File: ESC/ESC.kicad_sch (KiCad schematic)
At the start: 28 parts, among them J1 Screw_Terminal_01x05, J2 Screw_Terminal_01x03, J3 Screw_Terminal_01x02, Q1 IPP060N06N, Q2 IPP060N06N, Q3 IPP060N06N, Q4 IPP060N06N, Q5 IPP060N06N, Q6 IPP060N06N, Q7 BS250, U6 LM7805_TO220

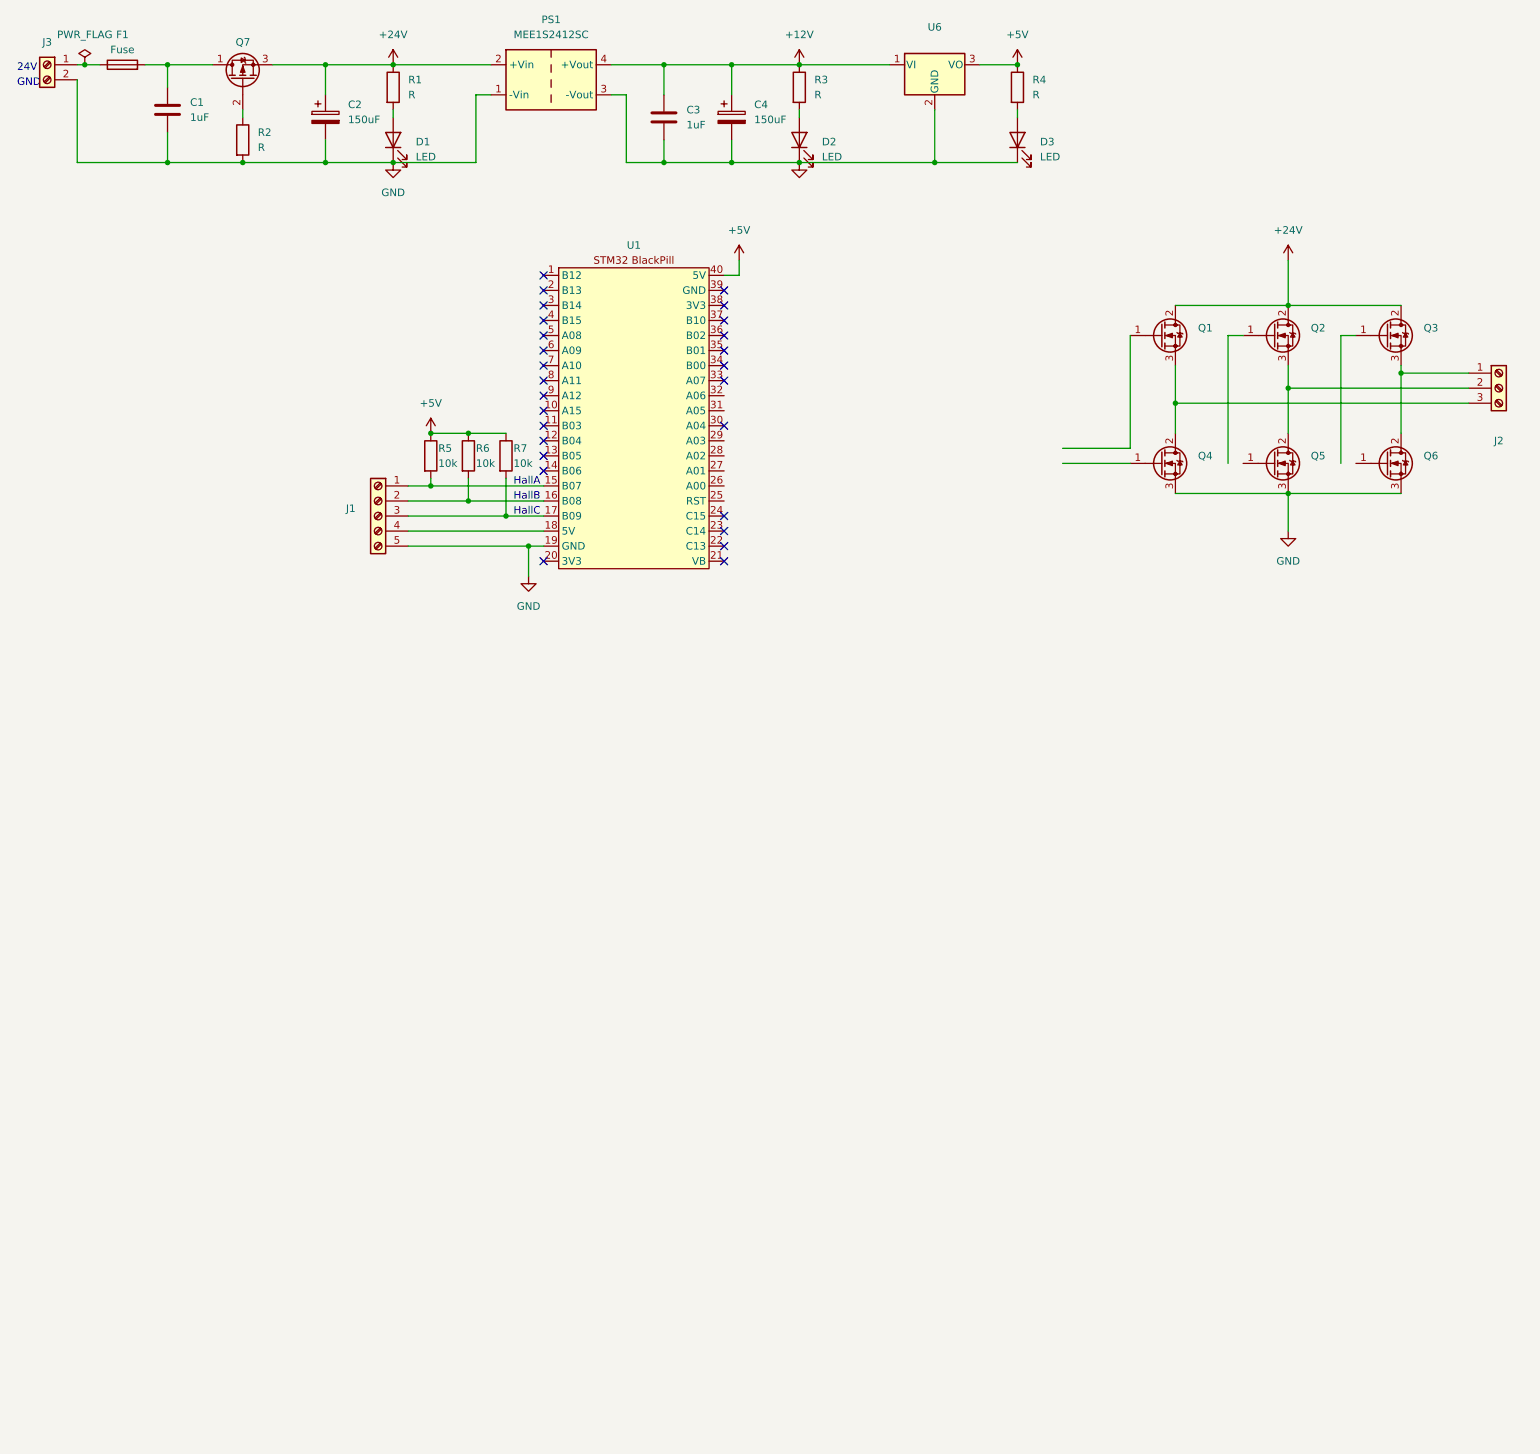
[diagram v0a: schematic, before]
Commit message: Added DRV8302
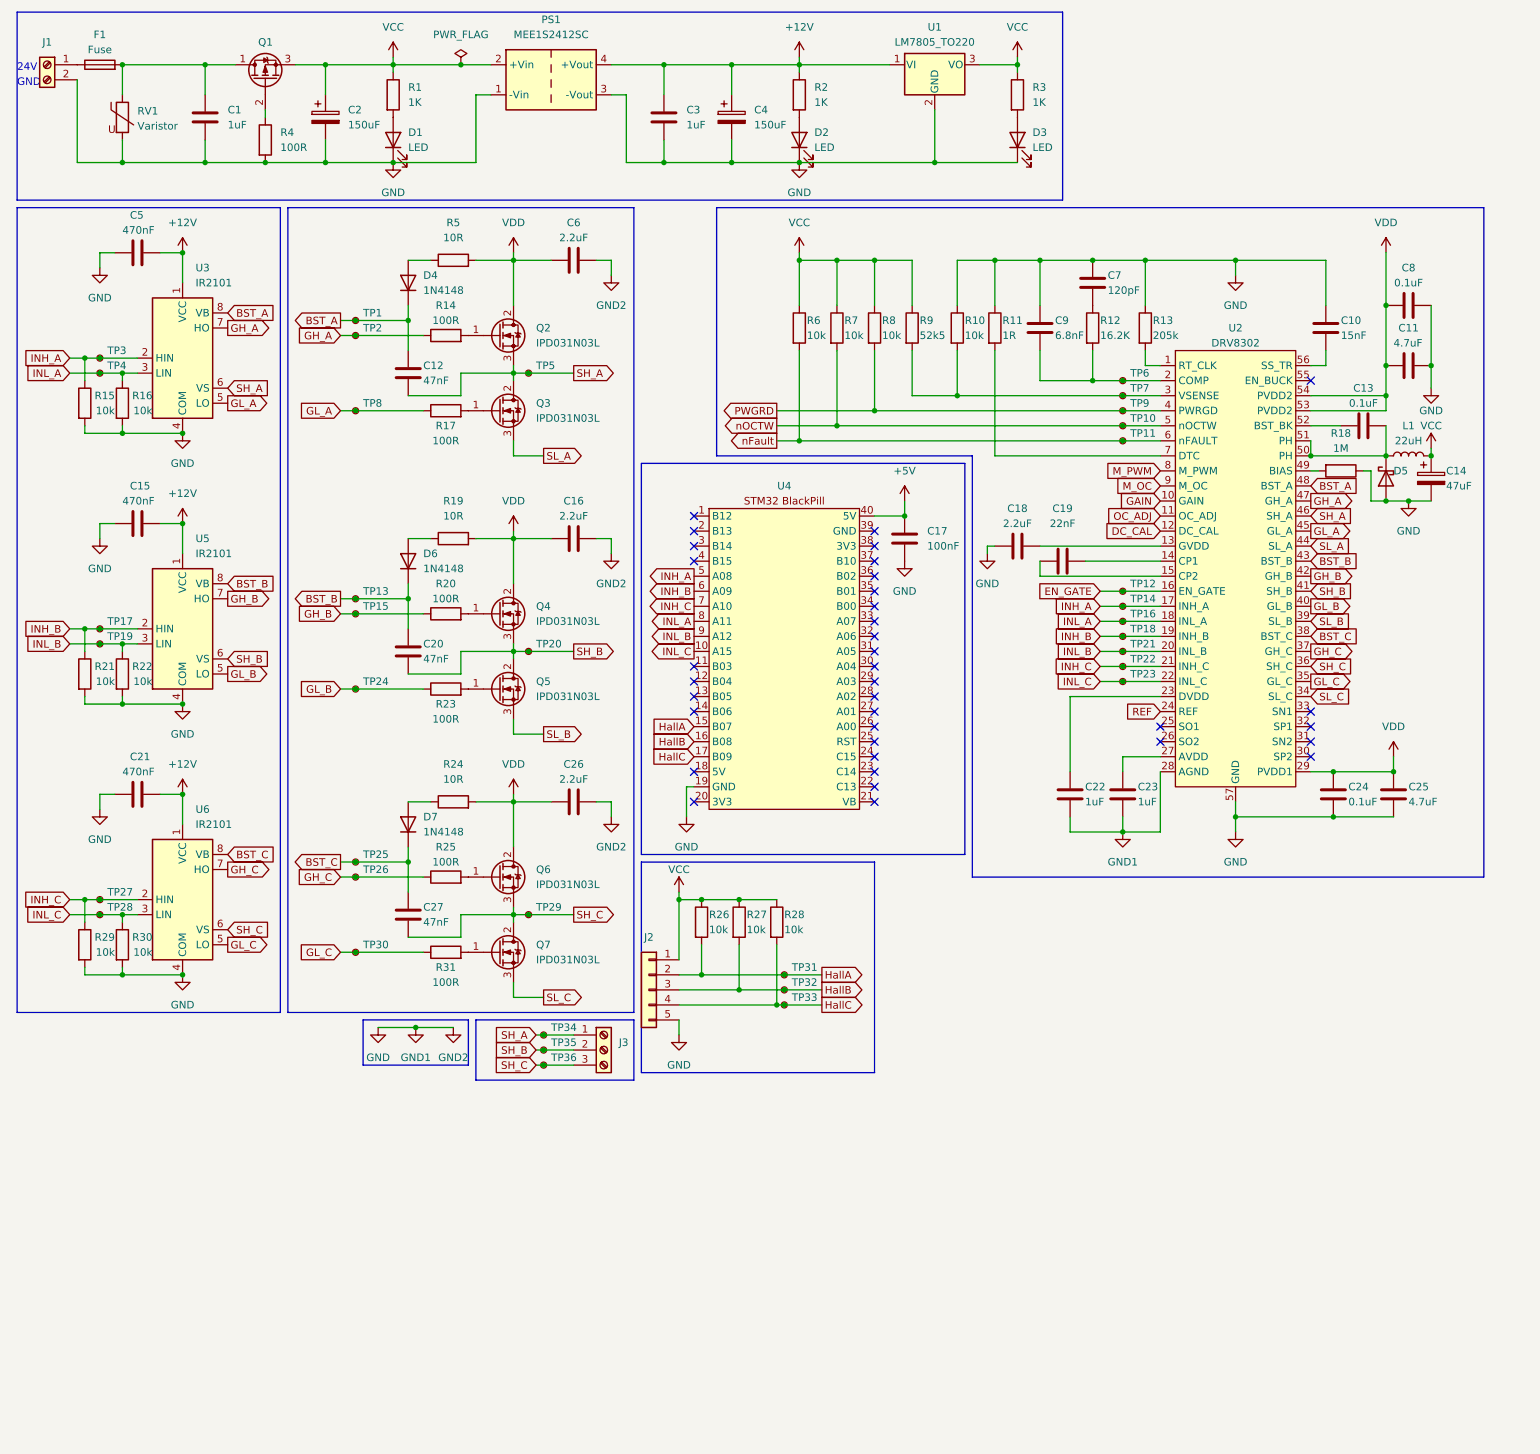
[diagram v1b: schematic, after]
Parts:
- removed J1: Screw_Terminal_01x05, symbol Connector:Screw_Terminal_01x05
- removed J2: Screw_Terminal_01x03, symbol Connector:Screw_Terminal_01x03
- removed Q1: IPP060N06N, Package_TO_SOT_THT:TO-220-3_Vertical, symbol Transistor_FET:IPP060N06N
- added C10: 15nF, symbol Device:C
- added C11, C25: 4.7uF, symbol Device:C
- added C12, C20, C27: 47nF, symbol Device:C
- added C13, C24, C8: 0.1uF, symbol Device:C
- added C14: 47uF, symbol Device:C_Polarized
- added C15, C21, C5: 470nF, symbol Device:C
- added C16, C18, C26, C6: 2.2uF, symbol Device:C
- added C17: 100nF, symbol Device:C
- added C19: 22nF, symbol Device:C
- added C22, C23: 1uF, symbol Device:C
- added C7: 120pF, symbol Device:C
- added C9: 6.8nF, symbol Device:C
- added D4, D6, D7: 1N4148, Diode_THT:D_DO-35_SOD27_P7.62mm_Horizontal, symbol Diode:1N4148
- added D5: D_Schottky, symbol Device:D_Schottky
- added J2: Conn_01x05, Connector_PinHeader_2.54mm:PinHeader_1x05_P2.54mm_Vertical, symbol Connector_Generic:Conn_01x05
- added J3: Screw_Terminal_01x03, symbol Connector:Screw_Terminal_01x03
- added L1: 22uH, symbol Device:L
- added Q7: IPD031N03L, Package_TO_SOT_SMD:TO-252-3_TabPin2, symbol Transistor_FET:IPP060N06N
- added R10, R15, R16, R21, R22, R29, R30, R6, R7, R8: 10k, symbol Device:R
- added R11: 1R, symbol Device:R
- added R12: 16.2K, symbol Device:R
- added R13: 205k, symbol Device:R
- added R14, R17, R20, R23, R25, R31: 100R, symbol Device:R
- added R18: 1M, symbol Device:R
- added R19, R24, R5: 10R, symbol Device:R
- added R9: 52k5, symbol Device:R
- added RV1: Varistor, symbol Device:Varistor
- added TP1, TP10, TP11, TP12, TP13, TP14, TP15, TP16, TP17, TP18, TP19, TP2, TP20, TP21, TP22, TP23, TP24, TP25, TP26, TP27, TP28, TP29, TP3, TP30, TP31, TP32, TP33, TP34, TP35, TP36, TP4, TP5, TP6, TP7, TP8, TP9: TestPoint_Small, symbol Connector:TestPoint_Small
- added U2: DRV8302, symbol Gate_Driver:DRV8302
- added U3, U5, U6: IR2101, symbol Driver_FET:IR2101
- Q2, Q3, Q4, Q5, Q6: value IPP060N06N -> IPD031N03L; footprint Package_TO_SOT_THT:TO-220-3_Vertical -> Package_TO_SOT_SMD:TO-252-3_TabPin2
- R1: value R -> 1K
- R2: renamed from R3; value R -> 1K
- R3: renamed from R4; value R -> 1K
- R4: renamed from R2; value R -> 100R
- renumbered J3 to J1, Q7 to Q1, R5 to R26, R6 to R27, R7 to R28, U6 to U1, U1 to U4
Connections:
- net +12V: now also C15.1, C21.1, C5.1, U3.1 (VCC), U5.1 (VCC), U6.1 (VCC)
- net +5V: now also C17.1; no longer R26.1, R27.1, R28.1, R3.1, U1.3 (VO)
- net GND: now also C10.1, C11.2, C14.2, C15.2, C16.2, C17.2, C18.1, C21.2, C22.1, C23.1, C24.2, C25.1, C26.2, C5.2, C6.2, C7.1, C8.1, C9.1, D5.2 (A), J2.5 (Pin_5), R10.1, R11.1, R13.1, R15.2, R16.2, R18.1, R21.2, R22.2, R29.2, R30.2, RV1.2, U2.28 (AGND), U2.57 (GND), U3.4 (COM), U5.4 (COM), U6.4 (COM); no longer Q4.3 (S), Q5.3 (S), Q6.3 (S)
- net at Q2.1 (G): now also R14.2
- net SH_A: now reaches Q2.3 (S)
- net SH_A: now also Q3.2 (D), C12.2, J3.1 (Pin_1), TP34.1, TP5.1, U2.46 (SH_A), U3.6 (VS); no longer Q5.2 (D)
- net at C1.1, F1.2, Q1.1 (D): now also RV1.1
- net at Q5.1 (G): now also R23.2
- net SL_A: now reaches Q3.3 (S)
- net SL_A: now also U2.44 (SL_A); no longer Q6.2 (D)
- net VDD: now reaches Q4.2 (D)
- net VDD: now also Q2.2 (D), Q6.2 (D), C11.1, C16.1, C24.1, C25.2, C26.1, C6.1, C8.2, R19.2, R24.2, R5.2, U2.29 (PVDD1), U2.53 (PVDD2), U2.54 (PVDD2)
- net at Q4.1 (G): now also R20.2
- net at Q3.1 (G): now also R17.2
- net HallB: now reaches R27.2, U4.16 (B08)
- net HallB: now also J2.3 (Pin_3), TP32.1
- net HallA: now reaches R26.2, U4.15 (B07)
- net HallA: now also J2.2 (Pin_2), TP31.1
- net HallC: now reaches R28.2, U4.17 (B09)
- net HallC: now also J2.4 (Pin_4), TP33.1
- net at Q6.1 (G): now also R25.2
- net INL_C: now reaches U4.10 (A15)
- net INL_C: now also R30.1, TP23.1, TP28.1, U2.22 (INL_C), U6.3 (LIN)
- net INH_A: now reaches U4.5 (A08)
- net INH_A: now also R15.1, TP14.1, TP3.1, U2.17 (INH_A), U3.2 (HIN)
- net INH_B: now reaches U4.6 (A09)
- net INH_B: now also R21.1, TP17.1, TP18.1, U2.19 (INH_B), U5.2 (HIN)
- net INH_C: now reaches U4.7 (A10)
- net INH_C: now also R29.1, TP22.1, TP27.1, U2.21 (INH_C), U6.2 (HIN)
- net INL_A: now reaches U4.8 (A11)
- net INL_A: now also R16.1, TP16.1, TP4.1, U2.18 (INL_A), U3.3 (LIN)
- net INL_B: now reaches U4.9 (A12)
- net INL_B: now also R22.1, TP19.1, TP21.1, U2.20 (INL_B), U5.3 (LIN)
- net +24V renamed VCC
- net VCC: now also R26.1, R27.1, R28.1, R3.1, U1.3 (VO), C14.1, J2.1 (Pin_1), L1.2, R6.1, R7.1, R8.1, R9.1; no longer Q2.2 (D), Q3.2 (D)
- new net: R10.2, R9.2, TP7.1, U2.3 (VSENSE)
- new net: C18.2, U2.13 (GVDD)
- new net: C9.2, R12.2, TP6.1, U2.2 (COMP)
- new net: C23.2, U2.27 (AVDD)
- new net: R18.2, U2.49 (BIAS)
- new net: Q7.1 (G), R31.2
- new net: C13.2, D5.1 (K), L1.1, U2.50 (PH), U2.51 (PH)
- new net: C22.2, U2.23 (DVDD)
- new net: C13.1, U2.52 (BST_BK)
- new net: D7.2 (A), R24.1
- new net: D6.2 (A), R19.1
- new net: C19.1, U2.15 (CP2)
- new net: C19.2, U2.14 (CP1)
- new net: R13.2, U2.1 (RT_CLK)
- new net: D4.2 (A), R5.1
- new net: C10.2, U2.56 (SS_TR)
- new net: R11.2, U2.7 (DTC)
- new net: C7.2, R12.1
- new net BST_A: C12.1, D4.1 (K), TP1.1, U2.48 (BST_A), U3.8 (VB)
- new net BST_B: C20.1, D6.1 (K), TP13.1, U2.43 (BST_B), U5.8 (VB)
- new net BST_C: C27.1, D7.1 (K), TP25.1, U2.38 (BST_C), U6.8 (VB)
- new net DC_CAL: U2.12 (DC_CAL)
- new net EN_GATE: TP12.1, U2.16 (EN_GATE)
- new net GAIN: U2.10 (GAIN)
- new net GH_A: R14.1, TP2.1, U2.47 (GH_A), U3.7 (HO)
- new net GH_B: R20.1, TP15.1, U2.42 (GH_B), U5.7 (HO)
- new net GH_C: R25.1, TP26.1, U2.37 (GH_C), U6.7 (HO)
- new net GL_A: R17.1, TP8.1, U2.45 (GL_A), U3.5 (LO)
- new net GL_B: R23.1, TP24.1, U2.40 (GL_B), U5.5 (LO)
- new net GL_C: R31.1, TP30.1, U2.35 (GL_C), U6.5 (LO)
- new net M_OC: U2.9 (M_OC)
- new net M_PWM: U2.8 (M_PWM)
- new net OC_ADJ: U2.11 (OC_ADJ)
- new net PWGRD: R8.2, TP9.1, U2.4 (PWRGD)
- new net REF: U2.24 (REF)
- new net SH_B: C20.2, J3.2 (Pin_2), Q4.3 (S), Q5.2 (D), TP20.1, TP35.1, U2.41 (SH_B), U5.6 (VS)
- new net SH_C: C27.2, J3.3 (Pin_3), Q6.3 (S), Q7.2 (D), TP29.1, TP36.1, U2.36 (SH_C), U6.6 (VS)
- new net SL_B: Q5.3 (S), U2.39 (SL_B)
- new net SL_C: Q7.3 (S), U2.34 (SL_C)
- new net nFault: R6.2, TP11.1, U2.6 (nFAULT)
- new net nOCTW: R7.2, TP10.1, U2.5 (nOCTW)
- no-connect marks 27 -> 36
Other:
- note removed: "HallA"
- note removed: "HallB"
- note removed: "HallC"
- moved on the sheet: C1, F1, Q1, R1, R2, R26, R27, R28, R3, R4, U4
